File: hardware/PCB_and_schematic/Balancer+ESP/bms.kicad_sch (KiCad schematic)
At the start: 115 parts, among them J10 UNUSED, J11 RS485, J12 Conn_01x03, J13 DC_RAIL, J15 FAN1, J16 FAN2, J8 ICP, J9 Conn_01x03, Q1 BC817, Q13 BC817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

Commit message: Ideal diode  + buck
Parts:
- removed J13: DC_RAIL, Connector_JST:JST_EH_B4B-EH-A_1x04_P2.50mm_Vertical, symbol Connector_Generic:Conn_01x04
- added C39, C40: 100n, Capacitor_SMD:C_0805_2012Metric_Pad1.18x1.45mm_HandSolder, symbol Device:C
- added C41, C42, C43, C44: 22u, Capacitor_Tantalum_SMD:CP_EIA-3528-21_Kemet-B, symbol Device:C_Polarized
- added D18: D_Schottky_Dual_CommonAnode_AKK_Parallel, symbol Device:D_Schottky_Dual_CommonAnode_AKK_Parallel
- added D19: 1N4148, Diode_THT:D_DO-35_SOD27_P7.62mm_Horizontal, symbol Diode:1N4148
- added J13: GND, Connector_Pin:Pin_D1.4mm_L8.5mm_W2.8mm_FlatFork, symbol Connector_Generic:Conn_01x01
- added J21: BATT, Connector_Pin:Pin_D1.4mm_L8.5mm_W2.8mm_FlatFork, symbol Connector_Generic:Conn_01x01
- added J22: OUT, Connector_Pin:Pin_D1.4mm_L8.5mm_W2.8mm_FlatFork, symbol Connector_Generic:Conn_01x01
- added J23: Batt, symbol Connector_Generic:Conn_01x02
- added L1: L, symbol Device:L
- added Q10, Q11, Q9: IRF540N, Package_TO_SOT_THT:TO-220-3_Vertical, symbol Transistor_FET:IRF540N
- added R79: 1k, Resistor_SMD:R_0805_2012Metric_Pad1.20x1.40mm_HandSolder, symbol Device:R
- added R80: 100A/75mV, symbol Device:R
- added R81, R82, R83, R84: 10K, Resistor_SMD:R_0805_2012Metric_Pad1.20x1.40mm_HandSolder, symbol Device:R
- added U20: AP74700, Package_TO_SOT_SMD:SOT-23-6_Handsoldering, symbol My-Lib:AP74700
- added U21: FAN7382, Package_DIP:DIP-8_W10.16mm_LongPads, symbol My-Lib:FAN7382
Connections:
- net +BATT_12V: now also C44.1, R82.1, U21.1 (VCC)
- net GND: now also C39.2, C41.2, C42.2, C43.2, C44.2, D18.1 (A), J13.1 (Pin_1), U20.2 (GND), U21.4 (GND)
- net GNDA: now also J23.2 (Pin_2)
- net PWM_OUT1: now also U10.21 (INT/AN12/RB0); no longer U10.13 (RC2/P1A/CCP1)
- net PWM_OUT2: now also U10.22 (P1C/AN10/RB1); no longer U10.12 (RC1/T1OSI/CCP2)
- net RA7: no longer U10.9 (CLKIN/OSC1/RA7)
- net RB1: no longer U10.22 (P1C/AN10/RB1)
- net R_shunt: now also C39.1, C40.1, C42.1, L1.2, Q10.3 (S), Q9.3 (S), R79.2, R80.2, U20.6 (ANODE)
- net at F4.2: now also J21.1 (Pin_1), R80.1
- net at F5.2: now also J23.1 (Pin_1)
- net RB0: no longer names the net of J10.2 (Pin_2)
- net RB0: no longer U10.21 (INT/AN12/RB0)
- new net: D19.2 (A), R82.2
- new net: D18.2 (K), D18.3 (K), L1.1, Q11.3 (S)
- new net: D19.1 (K), R84.1, U21.6 (VS), U21.8 (VB)
- new net: Q11.1 (G), R83.2, R84.2
- new net: R81.1, U21.2 (H_IN)
- new net: Q10.1 (G), Q9.1 (G), U20.5 (GATE)
- new net: R83.1, U21.7 (HO)
- new net: C40.2, U20.1 (VCP)
- new net DC_LINE_24V: C41.1, C43.1, J22.1 (Pin_1), Q10.2 (D), Q11.2 (D), Q9.2 (D), U20.4 (CATHODE)
- new net IDEAL_DIODE_DISABLE: R79.1, U10.9 (CLKIN/OSC1/RA7), U20.3 (EN)
- new net PWM_BUCK: R81.2, U10.12 (RC1/T1OSI/CCP2)

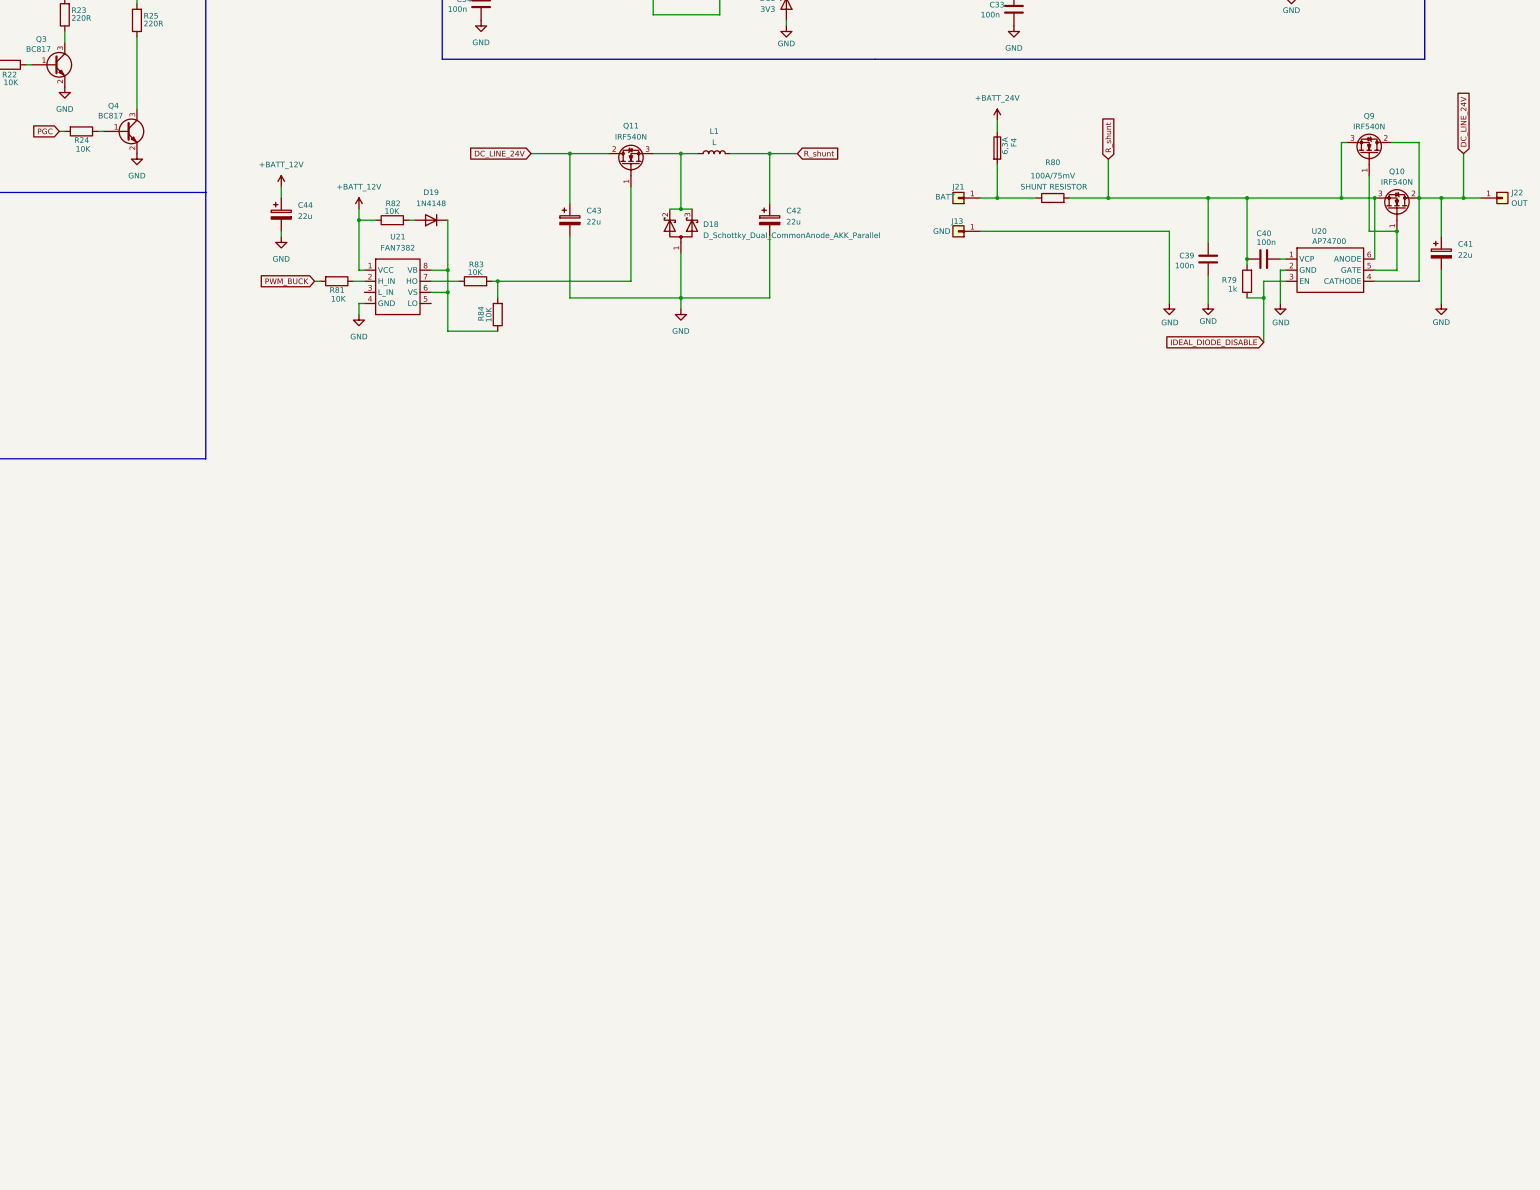
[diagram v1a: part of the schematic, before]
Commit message: bi-directional smps concept
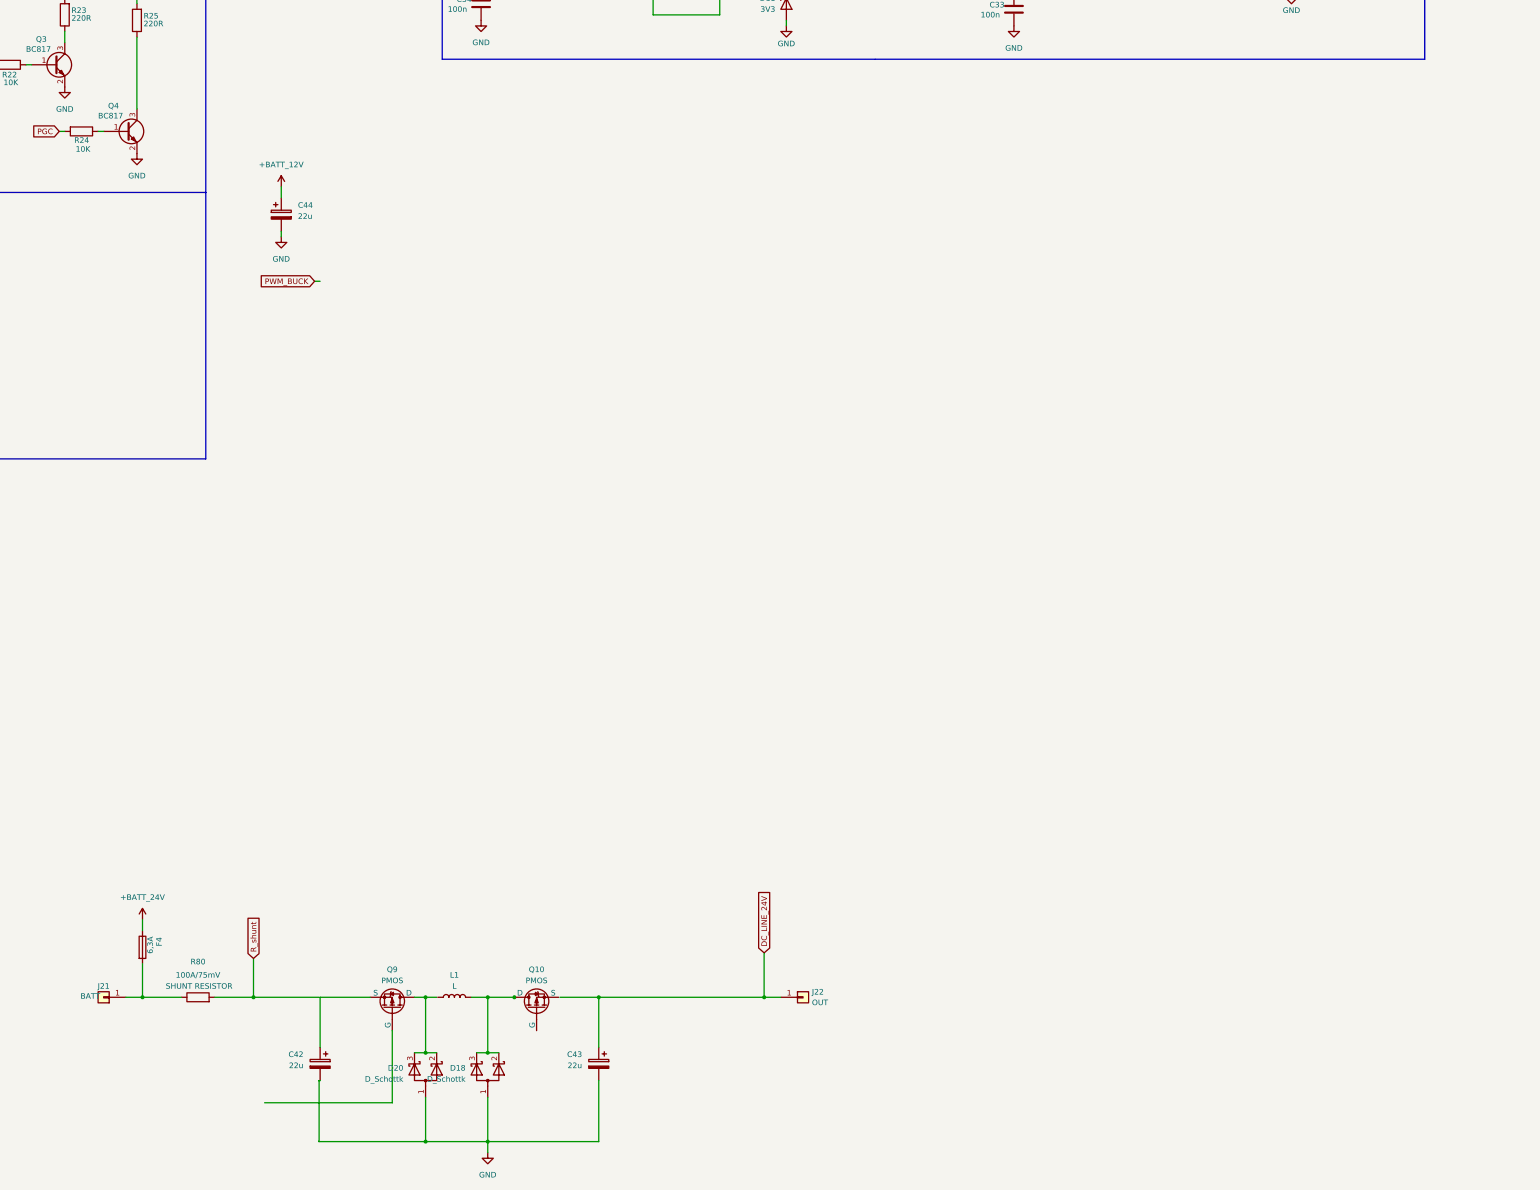
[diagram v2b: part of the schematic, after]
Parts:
- removed C39, C40: 100n, Capacitor_SMD:C_0805_2012Metric_Pad1.18x1.45mm_HandSolder, symbol Device:C
- removed C41: 22u, Capacitor_Tantalum_SMD:CP_EIA-3528-21_Kemet-B, symbol Device:C_Polarized
- removed D19: 1N4148, Diode_THT:D_DO-35_SOD27_P7.62mm_Horizontal, symbol Diode:1N4148
- removed J13: GND, Connector_Pin:Pin_D1.4mm_L8.5mm_W2.8mm_FlatFork, symbol Connector_Generic:Conn_01x01
- removed Q10, Q11, Q9: IRF540N, Package_TO_SOT_THT:TO-220-3_Vertical, symbol Transistor_FET:IRF540N
- removed R79: 1k, Resistor_SMD:R_0805_2012Metric_Pad1.20x1.40mm_HandSolder, symbol Device:R
- removed R81, R82, R83, R84: 10K, Resistor_SMD:R_0805_2012Metric_Pad1.20x1.40mm_HandSolder, symbol Device:R
- removed U20: AP74700, Package_TO_SOT_SMD:SOT-23-6_Handsoldering, symbol My-Lib:AP74700
- removed U21: FAN7382, Package_DIP:DIP-8_W10.16mm_LongPads, symbol My-Lib:FAN7382
- added D20: D_Schottk, symbol Device:D_Schottky_Dual_CommonAnode_AKK_Parallel
- added Q10, Q9: PMOS, symbol Simulation_SPICE:PMOS
- D18: value D_Schottky_Dual_CommonAnode_AKK_Parallel -> D_Schottk
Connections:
- net GND: now also D20.1 (A)
- net R_shunt: no longer C42.1, L1.2
- net at D18.2 (K), D18.3 (K), L1.1: now also Q10.1 (D)
- new net: D20.2 (K), D20.3 (K), Q9.1 (D)
- new net: C42.1, Q9.3 (S)
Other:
- moved on the sheet: C42, C43, D18, F4, J21, J22, L1, R80

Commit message: Add bidirectional smps concept, split bms schematic
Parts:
- removed C10, C11, C12, C14, C16, C18, C19, C31, C32, C33, C34, C4, C5, C6, C8: 100n, Capacitor_SMD:C_0805_2012Metric_Pad1.18x1.45mm_HandSolder, symbol Device:C
- removed C13: 10u, Capacitor_SMD:CP_Elec_6.3x4.5, symbol Device:C
- removed C15: 47u, Capacitor_THT:CP_Radial_D5.0mm_P2.00mm, symbol Device:C_Polarized
- removed C17: 47u/16V, Capacitor_THT:CP_Radial_D5.0mm_P2.00mm, symbol Device:C_Polarized
- removed C42, C43, C44: 22u, Capacitor_Tantalum_SMD:CP_EIA-3528-21_Kemet-B, symbol Device:C_Polarized
- removed C7: 100n, Resistor_SMD:R_0805_2012Metric_Pad1.20x1.40mm_HandSolder, symbol Device:C
- removed D10, D11, D12, D13, D5, D8, D9: 3V3, Diode_SMD:D_MiniMELF, symbol Device:D_Zener
- removed D14, D15, D3, D4: LED, LED_THT:LED_D5.0mm, symbol Device:LED
- removed D18, D20: D_Schottk, symbol Device:D_Schottky_Dual_CommonAnode_AKK_Parallel
- removed D6, D7: D_TVS, Diode_SMD:D_SMC, symbol Device:D_TVS
- removed F3: 2A, Fuse:Fuse_2512_6332Metric_Pad1.52x3.35mm_HandSolder, symbol Device:Polyfuse
- removed F4, F5: 6,3A, Fuse:Fuse_2512_6332Metric_Pad1.52x3.35mm_HandSolder, symbol Device:Fuse
- removed J10: UNUSED, Connector_PinHeader_2.54mm:PinHeader_1x06_P2.54mm_Vertical, symbol Connector_Generic:Conn_01x06
- removed J11: RS485, Connector_PinHeader_2.54mm:PinHeader_1x04_P2.54mm_Vertical, symbol Connector_Generic:Conn_01x04
- removed J12, J9: Conn_01x03, Connector_JST:JST_EH_B3B-EH-A_1x03_P2.50mm_Vertical, symbol Connector_Generic:Conn_01x03
- removed J15: FAN1, Connector_JST:JST_EH_B2B-EH-A_1x02_P2.50mm_Vertical, symbol Connector_Generic:Conn_01x02
- removed J16: FAN2, Connector_JST:JST_EH_B2B-EH-A_1x02_P2.50mm_Vertical, symbol Connector_Generic:Conn_01x02
- removed J21: BATT, Connector_Pin:Pin_D1.4mm_L8.5mm_W2.8mm_FlatFork, symbol Connector_Generic:Conn_01x01
- removed J22: OUT, Connector_Pin:Pin_D1.4mm_L8.5mm_W2.8mm_FlatFork, symbol Connector_Generic:Conn_01x01
- removed J23: Batt, symbol Connector_Generic:Conn_01x02
- removed J8: ICP, Connector_PinHeader_2.54mm:PinHeader_1x06_P2.54mm_Vertical, symbol Connector_Generic:Conn_01x06
- removed JP1: GND_Bridged, Jumper:SolderJumper-2_P1.3mm_Bridged2Bar_Pad1.0x1.5mm, symbol Jumper:Jumper_2_Bridged
- removed L1: L, symbol Device:L
- removed MOD2: LM2596-Step-Down, My-Footprints:MP1504_Mini_3A_Step_Down_Conv, symbol My-Lib:LM2596-Step-Down
- removed Q1, Q13, Q17, Q2, Q3, Q4: BC817, Package_TO_SOT_SMD:SOT-23, symbol Transistor_BJT:BC817
- removed Q10, Q9: PMOS, symbol Simulation_SPICE:PMOS
- removed Q14, Q15, Q19, Q20: NPN, Package_TO_SOT_THT:TO-220-3_Vertical, symbol Simulation_SPICE:NPN
- removed Q16, Q18: BD238, Package_TO_SOT_THT:TO-126-3_Vertical, symbol Transistor_BJT:BD238
- removed R15, R16, R41, R48, R49, R70: 0R, Resistor_SMD:R_0805_2012Metric_Pad1.20x1.40mm_HandSolder, symbol Device:R
- removed R18, R19, R23, R25: 220R, Resistor_SMD:R_0805_2012Metric_Pad1.20x1.40mm_HandSolder, symbol Device:R
- removed R20, R21, R22, R24, R68: 10K, Resistor_SMD:R_0805_2012Metric_Pad1.20x1.40mm_HandSolder, symbol Device:R
- removed R30, R36, R37, R45, R53, R63, R64, R67: 10k, Resistor_SMD:R_0805_2012Metric_Pad1.20x1.40mm_HandSolder, symbol Device:R
- removed R31: 6k8, Resistor_SMD:R_0805_2012Metric_Pad1.20x1.40mm_HandSolder, symbol Device:R
- removed R32: 1k3, Resistor_SMD:R_0805_2012Metric_Pad1.20x1.40mm_HandSolder, symbol Device:R
- removed R33, R35: 510R, Resistor_SMD:R_0805_2012Metric_Pad1.20x1.40mm_HandSolder, symbol Device:R
- removed R34, R38, R39, R40, R50, R51, R52: 120R, Resistor_SMD:R_0805_2012Metric_Pad1.20x1.40mm_HandSolder, symbol Device:R
- removed R42, R43, R44, R71: 0R1, Resistor_SMD:R_0805_2012Metric_Pad1.20x1.40mm_HandSolder, symbol Device:R
- removed R46, R56, R57, R60, R61, R62, R66: 1k, Resistor_SMD:R_0805_2012Metric_Pad1.20x1.40mm_HandSolder, symbol Device:R
- removed R54, R55, R58, R59: 15k, Resistor_SMD:R_0805_2012Metric_Pad1.20x1.40mm_HandSolder, symbol Device:R
- removed R65: 3k, Resistor_SMD:R_0805_2012Metric_Pad1.20x1.40mm_HandSolder, symbol Device:R
- removed R69: 3K, Resistor_SMD:R_0805_2012Metric_Pad1.20x1.40mm_HandSolder, symbol Device:R
- removed R80: 100A/75mV, symbol Device:R
- removed U10: PIC16F886-IP, Package_SO:SOIC-28W_7.5x17.9mm_P1.27mm, symbol MCU_Microchip_PIC16:PIC16F886-IP
- removed U11: ST485, Package_SO:SOIC-8_3.9x4.9mm_P1.27mm, symbol Interface_UART:ST485EBDR
- removed U12: INA226, Package_SO:VSSOP-10_3x3mm_P0.5mm, symbol Sensor_Energy:INA226
- removed U13, U15: LM324, Package_SO:SOIC-14_3.9x8.7mm_P1.27mm, symbol Amplifier_Operational:LM324
- removed U14: TL431LP, Package_TO_SOT_THT:TO-92_Inline, symbol Reference_Voltage:TL431LP
- removed U18: LM358, Package_SO:SO-8_3.9x4.9mm_P1.27mm, symbol Amplifier_Operational:LM358
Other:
- added sheet BMS_current_limiter (BMS_current_limiter.kicad_sch)
- added sheet BMS_current_sources_and_fans (BMS_current_sources_and_fans.kicad_sch)
- added sheet BMS_microcontroller (BMC_microcontroller.kicad_sch)
- note removed: "/RE - Receiver Output Enable Active LOW"
- note removed: "DC converter VBAT -> 5V"
- note removed: "INA226"
- note removed: "PIC16F819"
- note removed: "SHUNT RESISTOR 50A/25mV"
- note removed: "ST485"
- note removed: "STATUS DIODES"
